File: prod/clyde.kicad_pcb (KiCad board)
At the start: 2 copper layers, 114.3 x 82.4 mm, 26 parts

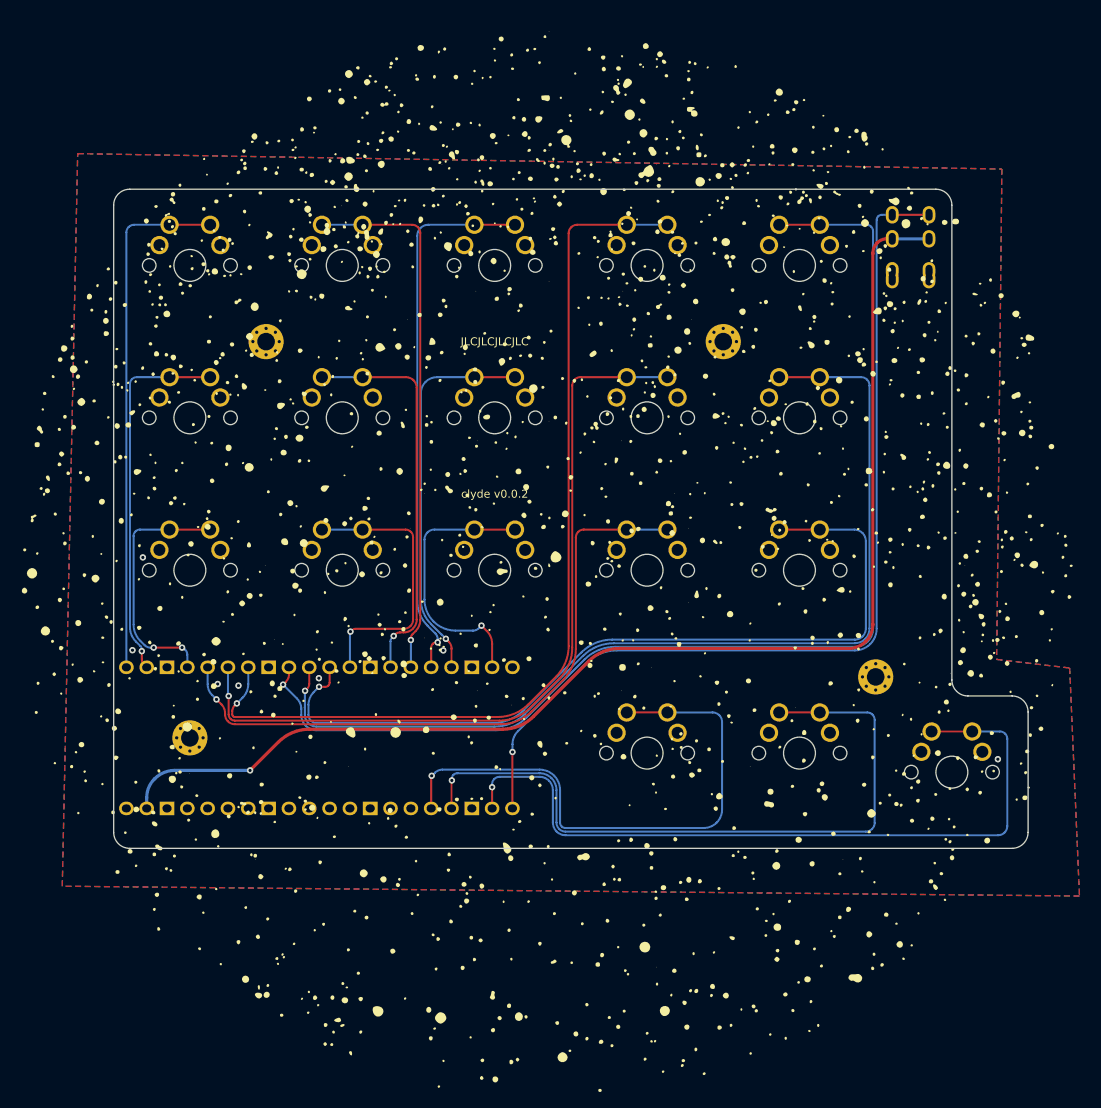
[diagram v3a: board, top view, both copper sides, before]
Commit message: rj45, PCB solder nuts, acrylic bottom plate
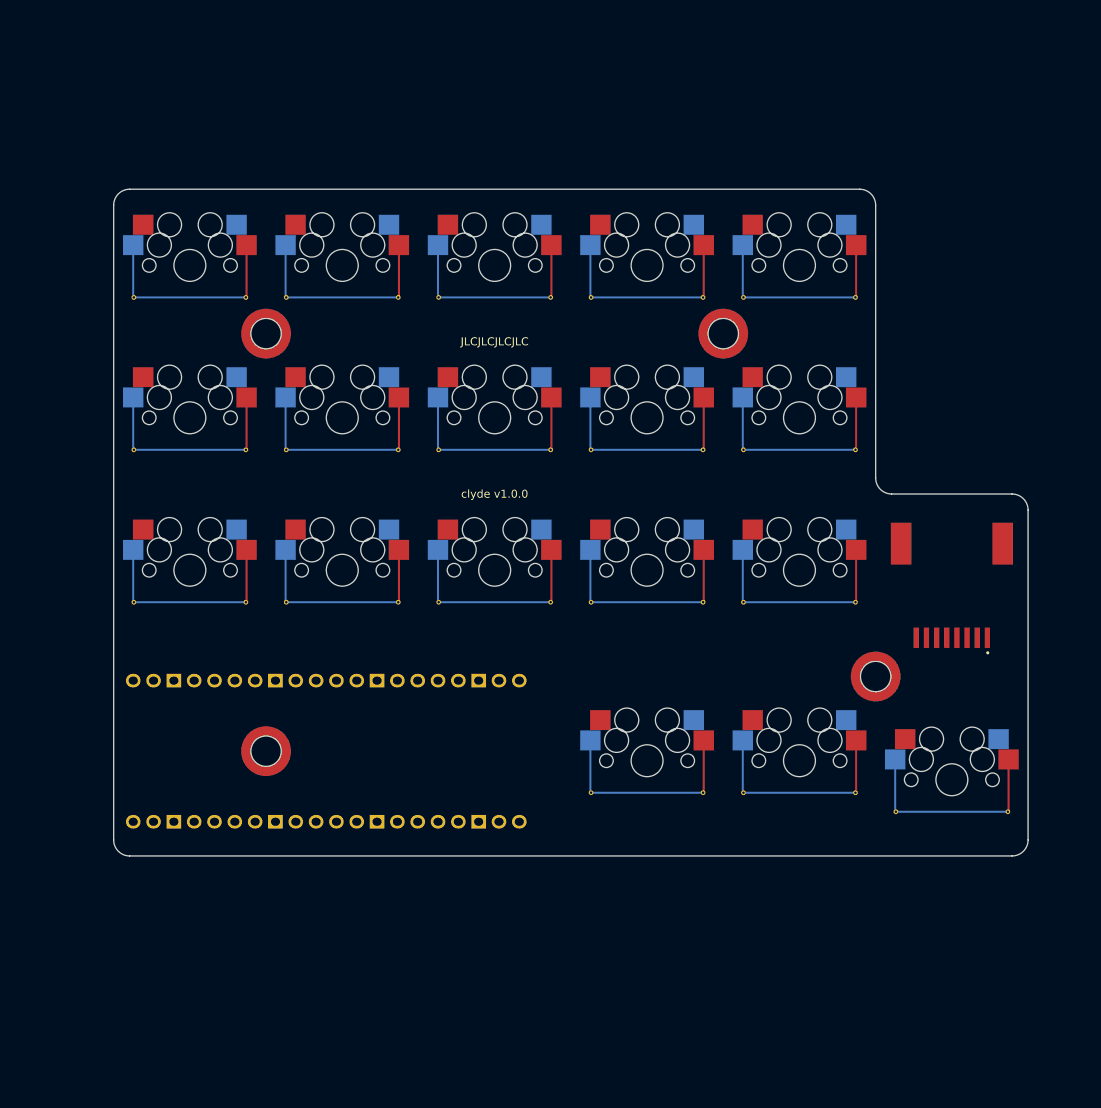
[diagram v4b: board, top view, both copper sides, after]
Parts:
- removed G*** (x2): LOGO, main:north-sky-silk
- removed TRRS1: TRRS-PJ-320A-dual, TRRS-PJ-320A-dual
- removed _4, _5, _6, _7: , MountingHole_2.2mm_M2_Pad_Via
- added ?: , SMTSO2020MTJ, F.Cu at (161.9, 122.8)
- added ?: , SMTSO2020MTJ, F.Cu at (161.9, 175.0)
- added ?: , 44144-0003, F.Cu at (247.7, 160.0)
- added ?: , SMTSO2020MTJ, F.Cu at (238.1, 165.7)
- added ?: , SMTSO2020MTJ, F.Cu at (219.1, 122.8)
- added REF**: VIA-0.6mm, VIA-0.6mm, F.Cu at (216.6, 156.4)
- added REF**: VIA-0.6mm, VIA-0.6mm, F.Cu at (159.4, 156.4)
- added REF**: VIA-0.6mm, VIA-0.6mm, F.Cu at (164.4, 137.3)
- added REF**: VIA-0.6mm, VIA-0.6mm, F.Cu at (164.4, 156.4)
- added REF**: VIA-0.6mm, VIA-0.6mm, F.Cu at (235.6, 118.3)
- added REF**: VIA-0.6mm, VIA-0.6mm, F.Cu at (202.6, 156.4)
- added REF**: VIA-0.6mm, VIA-0.6mm, F.Cu at (216.6, 137.3)
- added REF**: VIA-0.6mm, VIA-0.6mm, F.Cu at (235.6, 156.4)
- added REF**: VIA-0.6mm, VIA-0.6mm, F.Cu at (197.5, 137.3)
- added REF**: VIA-0.6mm, VIA-0.6mm, F.Cu at (197.5, 156.4)
- added REF**: VIA-0.6mm, VIA-0.6mm, F.Cu at (197.5, 118.3)
- added REF**: VIA-0.6mm, VIA-0.6mm, F.Cu at (202.6, 137.3)
- added REF**: VIA-0.6mm, VIA-0.6mm, F.Cu at (145.4, 137.3)
- added REF**: VIA-0.6mm, VIA-0.6mm, F.Cu at (235.6, 180.2)
- added REF**: VIA-0.6mm, VIA-0.6mm, F.Cu at (221.6, 137.3)
- added REF**: VIA-0.6mm, VIA-0.6mm, F.Cu at (254.7, 182.6)
- added REF**: VIA-0.6mm, VIA-0.6mm, F.Cu at (221.6, 180.2)
- added REF**: VIA-0.6mm, VIA-0.6mm, F.Cu at (235.6, 137.3)
- added REF**: VIA-0.6mm, VIA-0.6mm, F.Cu at (183.5, 137.3)
- added REF**: VIA-0.6mm, VIA-0.6mm, F.Cu at (178.4, 118.3)
- added REF**: VIA-0.6mm, VIA-0.6mm, F.Cu at (221.6, 156.4)
- added REF**: VIA-0.6mm, VIA-0.6mm, F.Cu at (164.4, 118.3)
- added REF**: VIA-0.6mm, VIA-0.6mm, F.Cu at (145.4, 156.4)
- added REF**: VIA-0.6mm, VIA-0.6mm, F.Cu at (183.5, 156.4)
- added REF**: VIA-0.6mm, VIA-0.6mm, F.Cu at (216.6, 118.3)
- added REF**: VIA-0.6mm, VIA-0.6mm, F.Cu at (159.4, 118.3)
- added REF**: VIA-0.6mm, VIA-0.6mm, F.Cu at (178.4, 137.3)
- added REF**: VIA-0.6mm, VIA-0.6mm, F.Cu at (202.6, 180.2)
- added REF**: VIA-0.6mm, VIA-0.6mm, F.Cu at (202.6, 118.3)
- added REF**: VIA-0.6mm, VIA-0.6mm, F.Cu at (178.4, 156.4)
- added REF**: VIA-0.6mm, VIA-0.6mm, F.Cu at (183.5, 118.3)
- added REF**: VIA-0.6mm, VIA-0.6mm, F.Cu at (240.7, 182.6)
- added REF**: VIA-0.6mm, VIA-0.6mm, F.Cu at (159.4, 137.3)
- added REF**: VIA-0.6mm, VIA-0.6mm, F.Cu at (221.6, 118.3)
- added REF**: VIA-0.6mm, VIA-0.6mm, F.Cu at (216.6, 180.2)
- added REF**: VIA-0.6mm, VIA-0.6mm, F.Cu at (145.4, 118.3)
- moved U0 1.87 mm to (169.4, 175.0)
- moved S16 0.95 mm to (209.6, 176.2)
- moved S17 0.95 mm to (228.6, 176.2)
- moved S18 0.95 mm to (247.7, 178.6)
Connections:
- S16 pad 1: thumbfan_near_home -> thumb_near_mods
- S17 pad 1: thumbfan_home_home -> thumb_middle_mods
- S18 pad 1: thumbfan_far_home -> thumb_far_mods
- U0 pad 10: matrix_inner_home -> matrix_middle_home
- U0 pad 11: matrix_inner_bottom -> matrix_middle_bottom
- U0 pad 12: matrix_ring_bottom -> matrix_index_top
- U0 pad 14: matrix_ring_home -> matrix_index_home
- U0 pad 15: matrix_ring_top -> matrix_index_bottom
- U0 pad 16: matrix_middle_top -> matrix_inner_bottom
- U0 pad 17: matrix_middle_home -> matrix_inner_home
- U0 pad 19: matrix_middle_bottom -> matrix_inner_top
- U0 pad 22: thumbfan_far_home -> GP17
- U0 pad 24: thumbfan_home_home -> thumb_far_mods
- U0 pad 25: thumbfan_near_home -> thumb_middle_mods
- U0 pad 26: GP20 -> thumb_near_mods
- U0 pad 5: matrix_index_bottom -> matrix_ring_top
- U0 pad 6: matrix_index_home -> matrix_ring_home
- U0 pad 7: matrix_index_top -> matrix_ring_bottom
- U0 pad 9: matrix_inner_top -> matrix_middle_top
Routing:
- net VSYS: track 155.7 -> 0.00 mm, vias 1 -> 0
- net matrix_inner_top: track 146.5 -> 27.2 mm, vias 1 -> 0
- net GP16: track 118.1 -> 0.00 mm, vias 1 -> 0
- net matrix_inner_home: track 124.6 -> 27.2 mm, vias 1 -> 0
- net thumbfan_far_home: track 95.3 -> 0.00 mm, vias 1 -> 0
- net matrix_index_top: track 117.8 -> 27.2 mm, vias 1 -> 0
- net thumbfan_home_home: track 88.8 -> 0.00 mm, vias 1 -> 0
- net matrix_inner_bottom: track 104.9 -> 27.2 mm, vias 1 -> 0
- net matrix_index_home: track 99.1 -> 27.2 mm, vias 1 -> 0
- net thumbfan_near_home: track 71.3 -> 0.00 mm, vias 1 -> 0
- net matrix_index_bottom: track 81.8 -> 27.2 mm, vias 1 -> 0
- net matrix_middle_top: track 68.3 -> 27.2 mm, vias 1 -> 0
- net matrix_ring_top: track 67.5 -> 27.2 mm, vias 1 -> 0
- net matrix_pinky_top: track 65.4 -> 27.2 mm
- net thumb_middle_mods: track 0.00 -> 27.2 mm
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- removed copper zone on B.Cu, net GND
- removed copper zone on F.Cu, net GND
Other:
- board size 114.3 x 82.4 mm -> 114.3 x 83.3 mm
- board text added: "clyde v1.0.0"
- board text removed: "clyde v0.0.2"
